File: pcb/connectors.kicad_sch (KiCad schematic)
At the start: 14 parts, among them J1 TC2030, J2 GPIO, J3 Hirose_FH12-16S, U1 CAT24C256

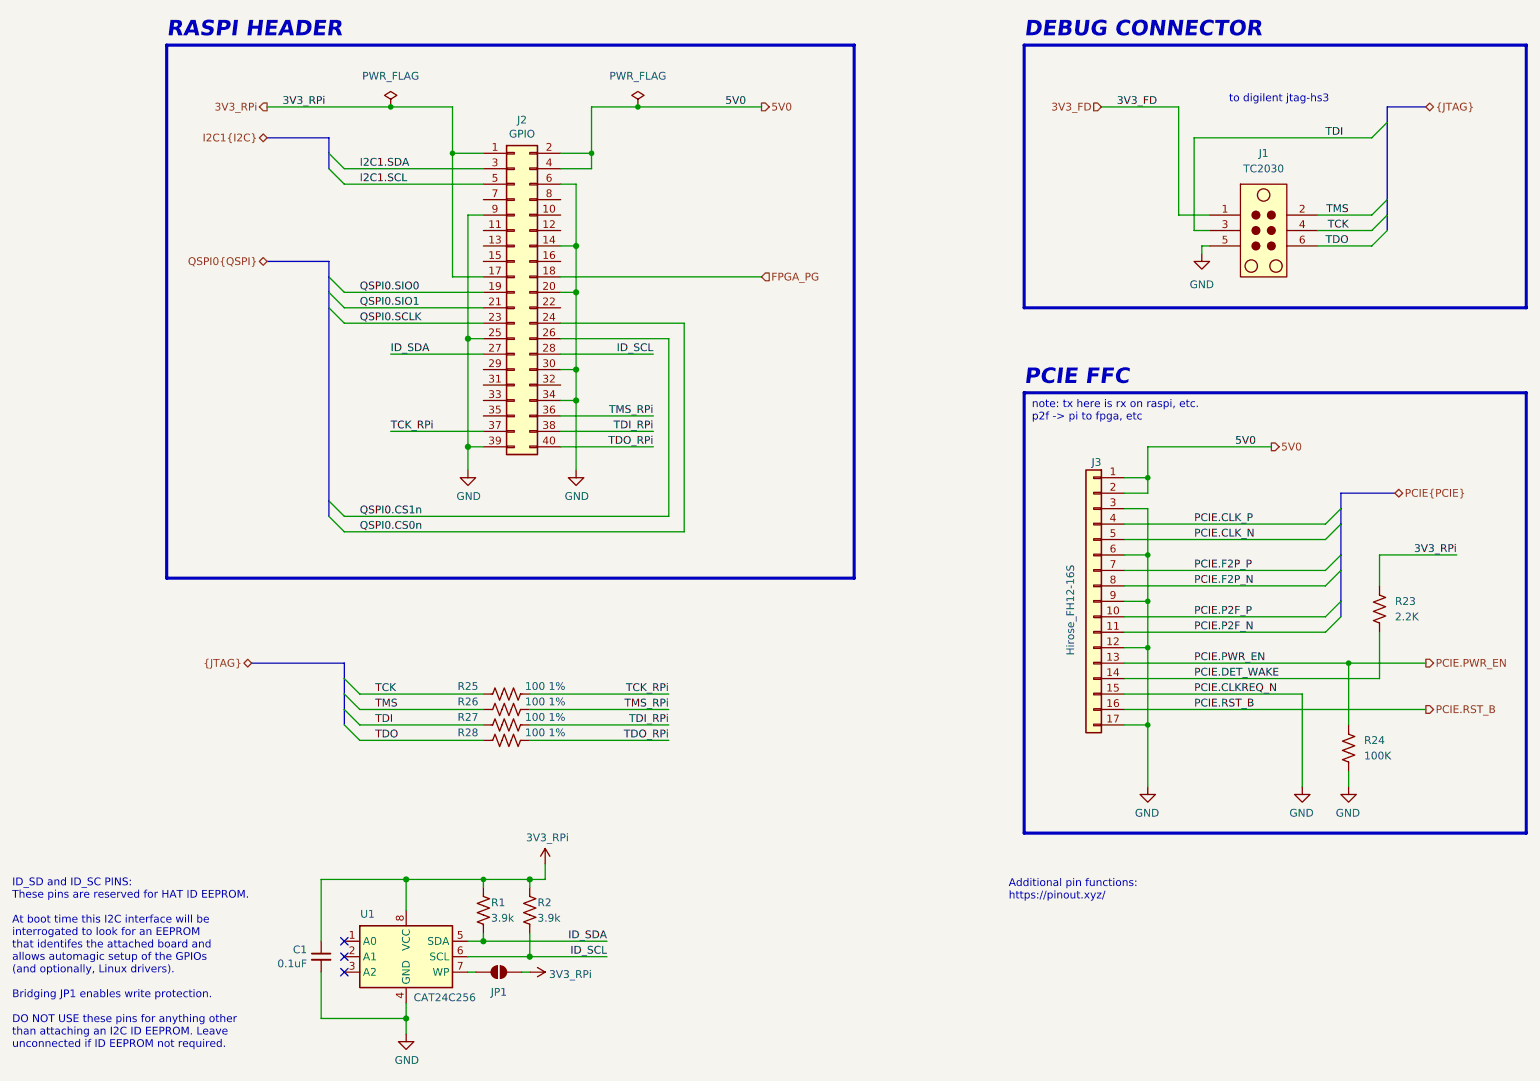
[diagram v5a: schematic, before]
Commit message: routing done! pcb/v1.0 almost ready for release added series resistors from raspi spi to qspi, all nets connected and routed
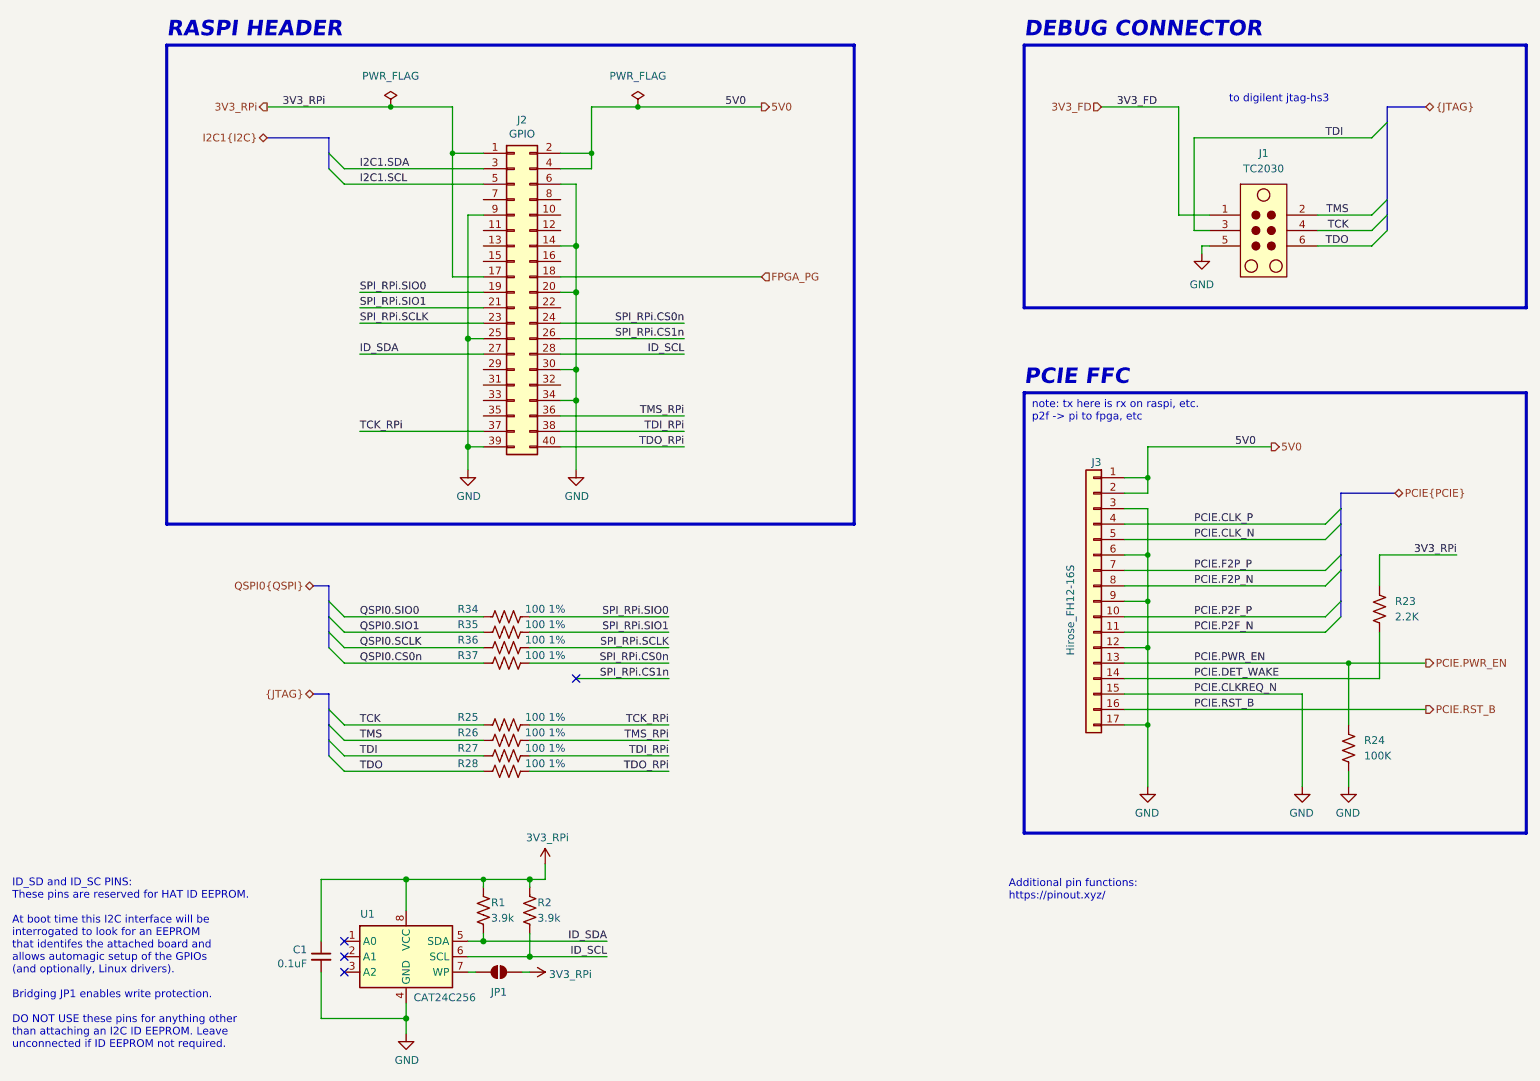
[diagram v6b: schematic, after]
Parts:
- added R34, R35, R36, R37: 100 1%, Resistor_SMD:R_0402_1005Metric, symbol library:R_US
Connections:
- net QSPI0.CS0n: now also R37.1; no longer J2.24 (Pin_24)
- net QSPI0.SCLK: now also R36.1; no longer J2.23 (Pin_23)
- net QSPI0.SIO0: now also R34.1; no longer J2.19 (Pin_19)
- net QSPI0.SIO1: now also R35.1; no longer J2.21 (Pin_21)
- net QSPI0.CS1n renamed SPI_RPi.CS1n
- new net SPI_RPi.CS0n: J2.24 (Pin_24), R37.2
- new net SPI_RPi.SCLK: J2.23 (Pin_23), R36.2
- new net SPI_RPi.SIO0: J2.19 (Pin_19), R34.2
- new net SPI_RPi.SIO1: J2.21 (Pin_21), R35.2
- no-connect marks 3 -> 4
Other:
- moved on the sheet: R25, R26, R27, R28

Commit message: complete! added and prettied up silkscreen
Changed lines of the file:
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@@
 	)
 	(no_connect
-		(at 106.68 134.62)
+		(at 124.46 78.74)
 	)
 	(bus_entry
@@
 		(pts
 			(xy 232.41 114.3) (xy 232.41 116.84)
-		)
-		(stroke
-			(width 0)
-			(type default)
-		)
-	)
-	(wire
-		(pts
-			(xy 106.68 134.62) (xy 121.9576 134.62)
 		)
 		(stroke
@@
 		)
 	)
-	(label "SPI_RPi.CS1n"
-		(at 121.9576 134.62 180)
-		(effects
-			(font
-				(size 1.27 1.27)
-			)
-			(justify right bottom)
-		)
-	)

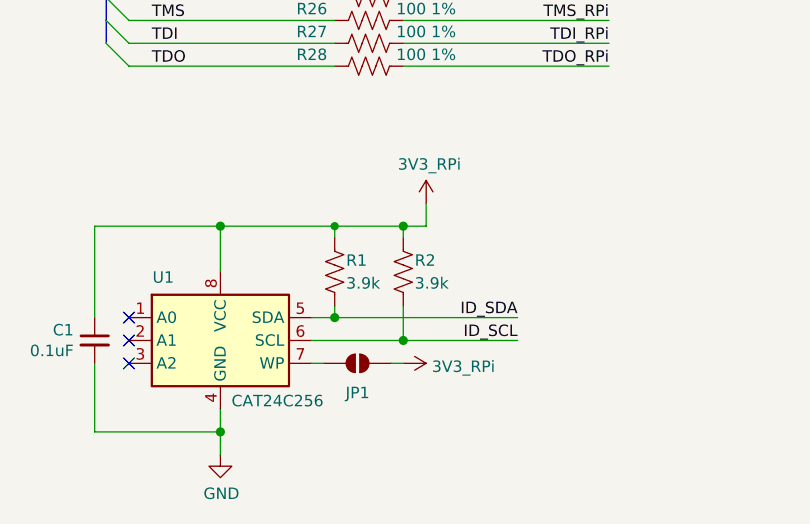
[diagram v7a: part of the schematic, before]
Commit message: added jlc fab
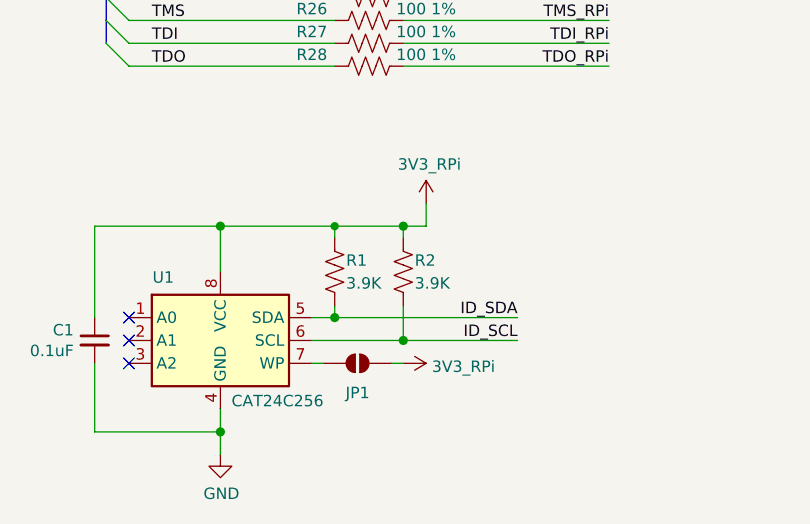
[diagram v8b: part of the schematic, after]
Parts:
- R1, R2: value 3.9k -> 3.9K
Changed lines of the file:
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@@
 			)
 		)
-		(property "Value" "3.9k"
+		(property "Value" "3.9K"
 			(at 92.71 173.99 0)
 			(show_name no)
@@
 			)
 		)
-		(property "Value" "3.9k"
+		(property "Value" "3.9K"
 			(at 100.33 173.99 0)
 			(show_name no)
